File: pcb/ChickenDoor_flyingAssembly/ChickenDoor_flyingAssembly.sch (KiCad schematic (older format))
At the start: 23 parts

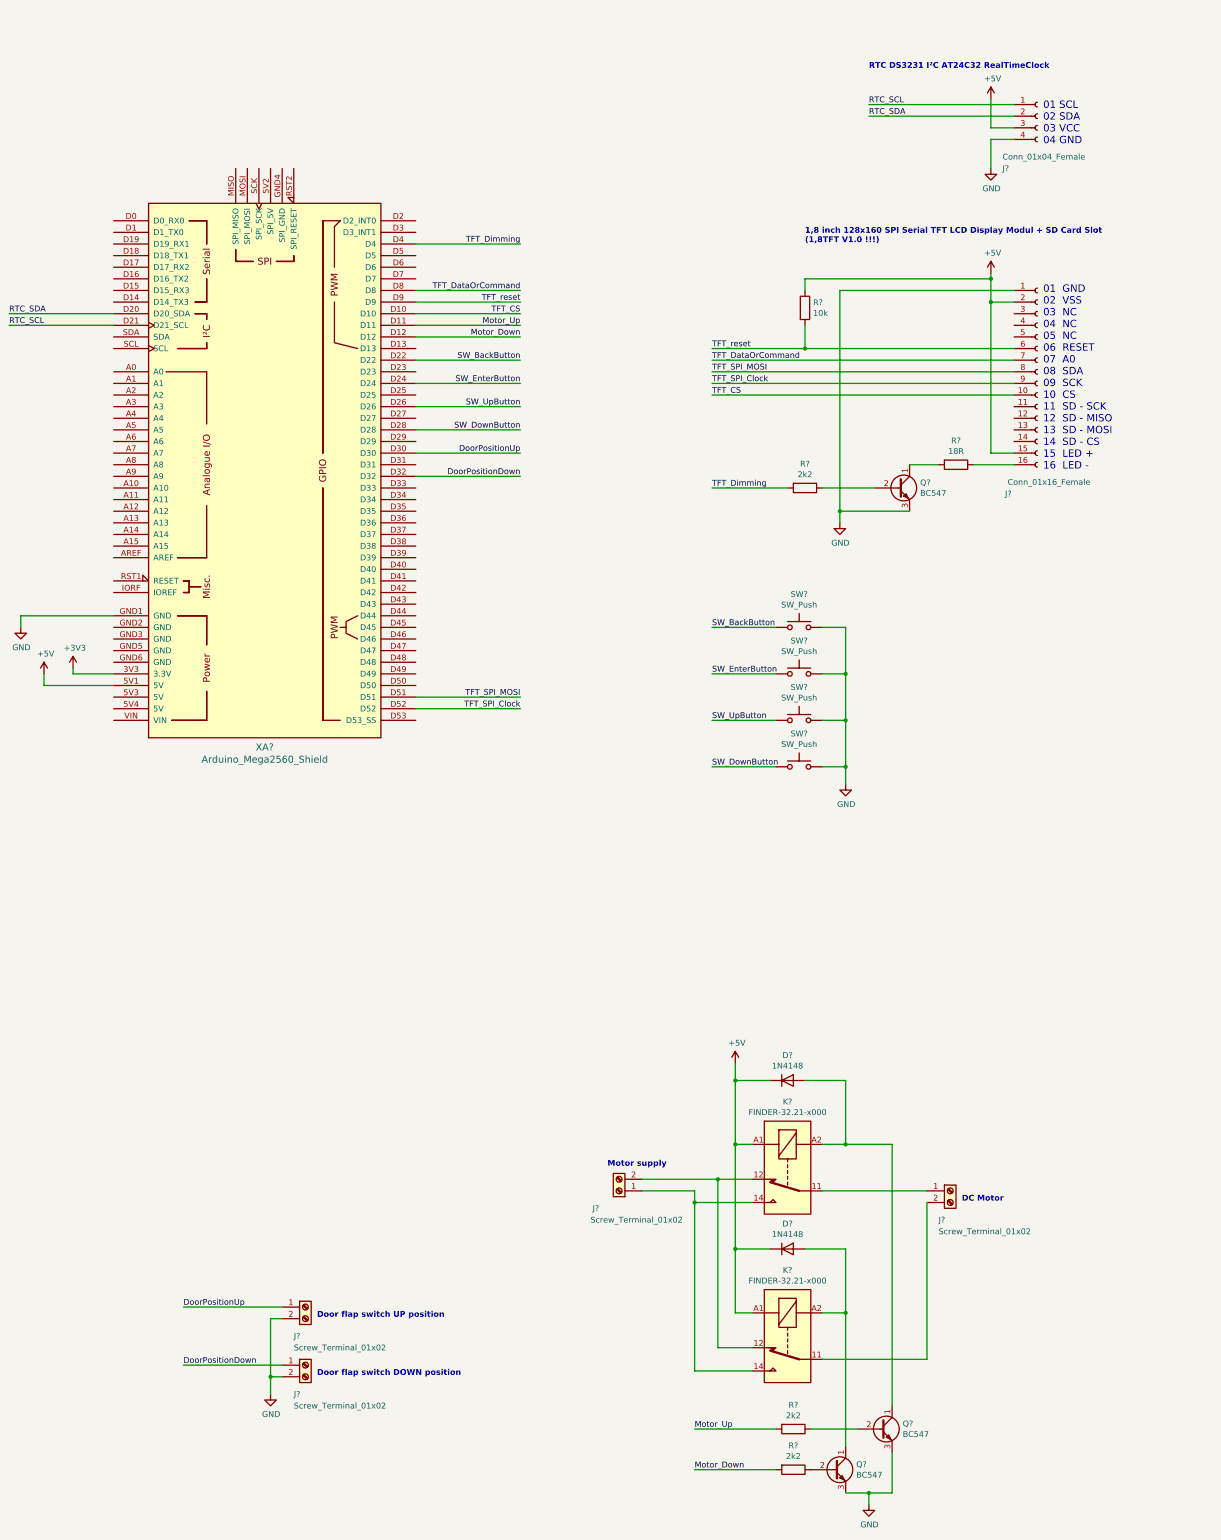
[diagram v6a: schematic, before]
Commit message: First version of the motor steering implemented. But without timeout handling and initialization run.
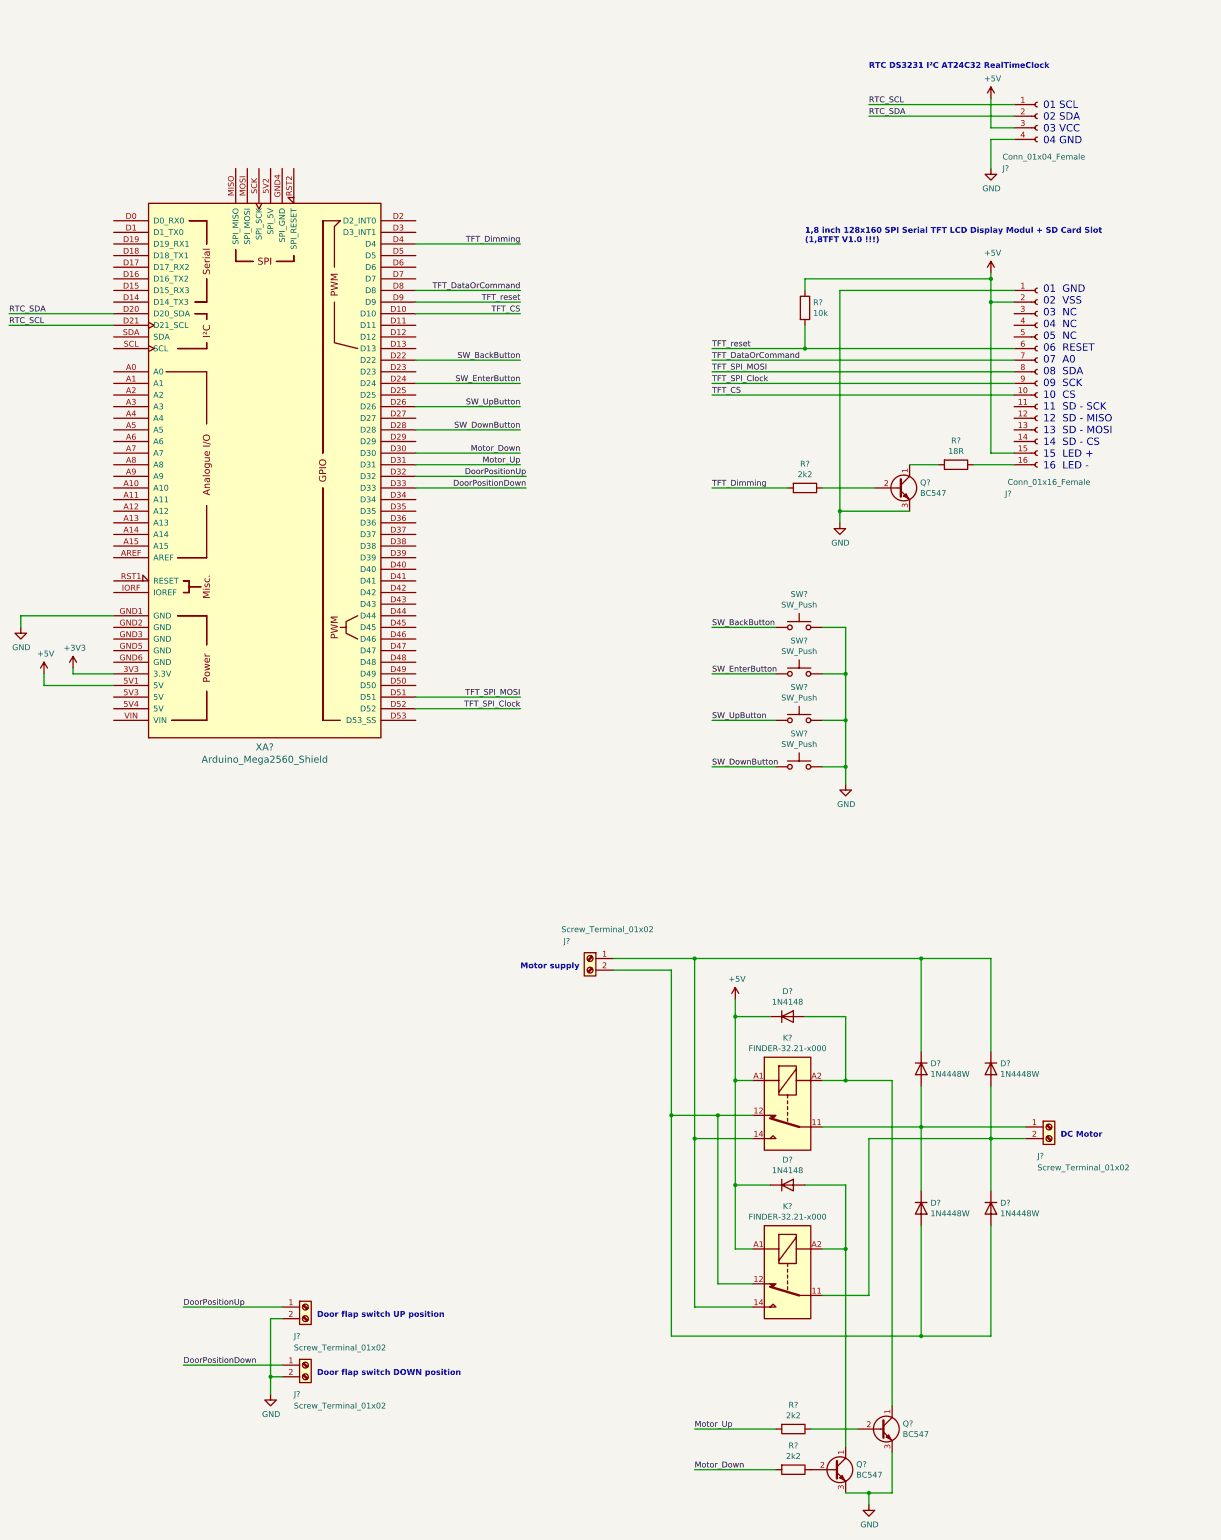
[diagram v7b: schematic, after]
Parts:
- added D? (x4): 1N4448W, Diode_SMD:D_SOD-123, symbol Diode:1N4448W
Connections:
- net DoorPositionDown: now also XA?.D33; no longer XA?.D32
- net DoorPositionUp: now also XA?.D32; no longer XA?.D30
- net Motor_Down: now also XA?.D30; no longer XA?.D12
- net Motor_Up: now also XA?.D31; no longer XA?.D11
- net at J?.1 (Pin_1), K?.11: now also D?.1 (K), D?.2 (A)
- net at J?.2 (Pin_2), K?.12, K?.12: now also D?.2 (A), D?.2 (A)
- net at J?.1 (Pin_1), K?.14, K?.14: now also D?.1 (K), D?.1 (K)
- net at J?.2 (Pin_2), K?.11: now also D?.1 (K), D?.2 (A)
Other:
- moved on the sheet: D?, J?, K?
